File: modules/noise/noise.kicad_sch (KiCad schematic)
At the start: 25 parts, among them U1 ATtiny1616-M, U2 MCP6002-xSN, U3 MCP6002-xSN

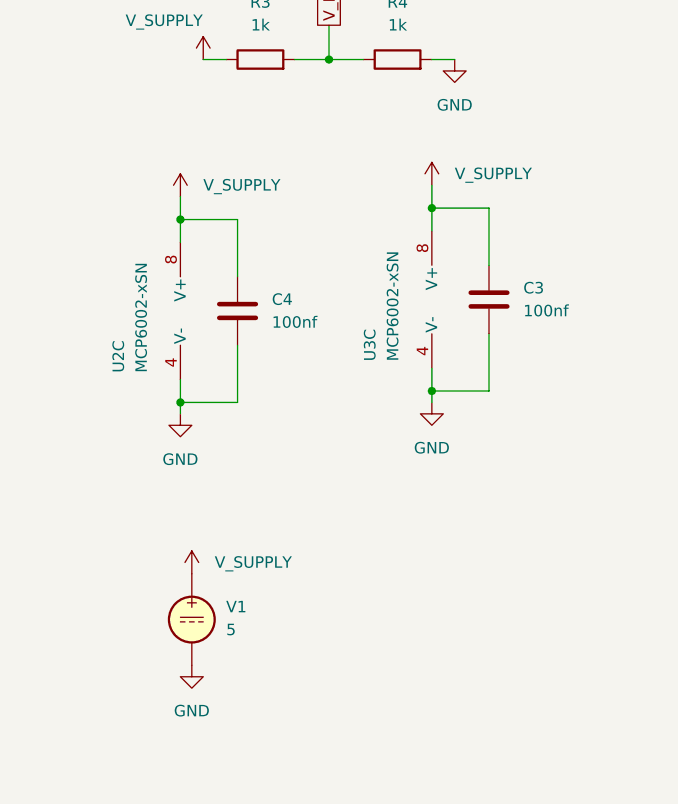
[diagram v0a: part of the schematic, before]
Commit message: Implement the PCB routing
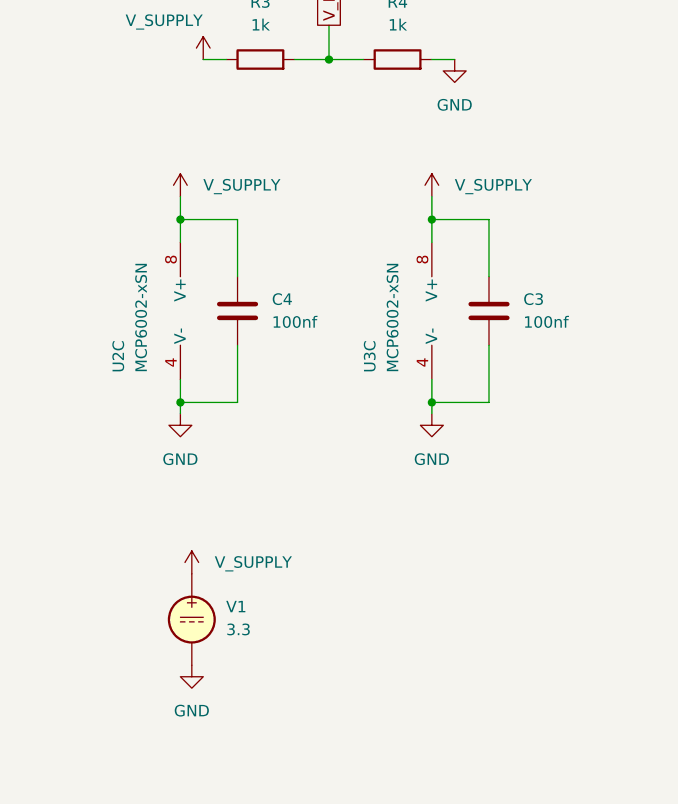
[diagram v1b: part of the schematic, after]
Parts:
- C1: footprint (none) -> Capacitor_SMD:C_1206_3216Metric
- C2, C3, C4, C5, C6: footprint (none) -> Capacitor_SMD:C_0402_1005Metric
- R1, R2, R3, R4, R5, R6, R7, R8: footprint (none) -> Resistor_SMD:R_0402_1005Metric
- RV1, RV2, RV3: footprint (none) -> BreadModular_Pots:Potentiometer_RV09
- U2, U3: footprint (none) -> Package_SO:SOIC-8-1EP_3.9x4.9mm_P1.27mm_EP2.29x3mm
- V1: value 5 -> 3.3
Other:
- moved on the sheet: C3, U3C
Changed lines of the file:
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@@
 	)
 	(junction
-		(at 260.35 123.19)
+		(at 260.35 124.46)
 		(diameter 0)
 		(color 0 0 0 0)
@@
 	)
 	(junction
-		(at 260.35 102.87)
+		(at 260.35 104.14)
 		(diameter 0)
 		(color 0 0 0 0)
@@
 	(wire
 		(pts
-			(xy 260.35 123.19) (xy 260.35 124.46)
+			(xy 260.35 124.46) (xy 260.35 125.73)
 		)
 		(stroke
@@
 	(wire
 		(pts
-			(xy 266.7 109.22) (xy 266.7 102.87)
+			(xy 266.7 110.49) (xy 266.7 104.14)
 		)
 		(stroke
@@
 	(wire
 		(pts
-			(xy 260.35 120.65) (xy 260.35 123.19)
+			(xy 260.35 121.92) (xy 260.35 124.46)
 		)
 		(stroke
@@
 	(wire
 		(pts
-			(xy 266.7 102.87) (xy 260.35 102.87)
+			(xy 266.7 104.14) (xy 260.35 104.14)
 		)
 		(stroke
@@
 	(wire
 		(pts
-			(xy 260.35 100.33) (xy 260.35 102.87)
+			(xy 260.35 101.6) (xy 260.35 104.14)
 		)
 		(stroke
@@
 	(wire
 		(pts
-			(xy 266.7 123.19) (xy 260.35 123.19)
+			(xy 266.7 124.46) (xy 260.35 124.46)
 		)
 		(stroke
@@
 	(wire
 		(pts
-			(xy 260.35 102.87) (xy 260.35 105.41)
+			(xy 260.35 104.14) (xy 260.35 106.68)
 		)
 		(stroke
@@
 	(wire
 		(pts
-			(xy 266.7 116.84) (xy 266.7 123.19)
+			(xy 266.7 118.11) (xy 266.7 124.46)
 		)
 		(stroke
@@
 			)
 		)
-		(property "Footprint" ""
+		(property "Footprint" "Resistor_SMD:R_0402_1005Metric"
 			(at 241.3 88.138 90)
 			(effects
@@
 			)
 		)
-		(property "Footprint" ""
+		(property "Footprint" "Resistor_SMD:R_0402_1005Metric"
 			(at 97.79 133.858 90)
 			(effects
@@
 			)
 		)
-		(property "Value" "5"
+		(property "Value" "3.3"
 			(at 237.49 149.7301 0)
 			(effects
@@
 			)
 		)
-		(property "Footprint" ""
+		(property "Footprint" "BreadModular_Pots:Potentiometer_RV09"
 			(at 88.9 125.73 0)
 			(effects
@@
 			)
 		)
-		(property "Footprint" ""
+		(property "Footprint" "Resistor_SMD:R_0402_1005Metric"
 			(at 83.82 48.768 90)
 			(effects
@@
 			)
 		)
-		(property "Footprint" ""
+		(property "Footprint" "Package_SO:SOIC-8-1EP_3.9x4.9mm_P1.27mm_EP2.29x3mm"
 			(at 124.46 110.49 0)
 			(effects
@@
 			)
 		)
-		(property "Footprint" ""
+		(property "Footprint" "Resistor_SMD:R_0402_1005Metric"
 			(at 148.59 163.068 90)
 			(effects
@@
 			)
 		)
-		(property "Footprint" ""
+		(property "Footprint" "Package_SO:SOIC-8-1EP_3.9x4.9mm_P1.27mm_EP2.29x3mm"
 			(at 53.34 107.95 0)
 			(effects
@@
 			)
 		)
-		(property "Footprint" ""
+		(property "Footprint" "Capacitor_SMD:C_0402_1005Metric"
 			(at 80.01 106.9848 0)
 			(effects
@@
 			)
 		)
-		(property "Footprint" ""
+		(property "Footprint" "Capacitor_SMD:C_0402_1005Metric"
 			(at 237.7948 110.49 0)
 			(effects
@@
 			)
 		)
-		(property "Footprint" ""
+		(property "Footprint" "Resistor_SMD:R_0402_1005Metric"
 			(at 83.82 29.718 90)
 			(effects
@@
 	(symbol
 		(lib_id "Amplifier_Operational:MCP6002-xSN")
-		(at 262.89 113.03 0)
+		(at 262.89 114.3 0)
 		(unit 3)
 		(exclude_from_sim no)
@@
 		(dnp no)
 		(property "Reference" "U3"
-			(at 253.492 119.888 90)
+			(at 253.492 121.158 90)
 			(effects
 				(font
@@
 		)
 		(property "Value" "MCP6002-xSN"
-			(at 256.032 119.888 90)
+			(at 256.032 121.158 90)
 			(effects
 				(font
@@
 			)
 		)
-		(property "Footprint" ""
-			(at 262.89 113.03 0)
+		(property "Footprint" "Package_SO:SOIC-8-1EP_3.9x4.9mm_P1.27mm_EP2.29x3mm"
+			(at 262.89 114.3 0)
 			(effects
 				(font
@@
 		)
 		(property "Datasheet" "http://ww1.microchip.com/downloads/en/DeviceDoc/21733j.pdf"
-			(at 262.89 113.03 0)
+			(at 262.89 114.3 0)
 			(effects
 				(font
@@
 		)
 		(property "Description" "1MHz, Low-Power Op Amp, SOIC-8"
-			(at 262.89 113.03 0)
+			(at 262.89 114.3 0)
 			(effects
 				(font
@@
 			)
 		)
-		(property "Footprint" ""
+		(property "Footprint" "BreadModular_Pots:Potentiometer_RV09"
 			(at 85.09 66.04 0)
 			(effects
@@
 	(symbol
 		(lib_id "power:GND")
-		(at 260.35 124.46 0)
+		(at 260.35 125.73 0)
 		(unit 1)
 		(exclude_from_sim no)
@@
 		(dnp no)
 		(property "Reference" "#PWR012"
-			(at 260.35 130.81 0)
+			(at 260.35 132.08 0)
 			(effects
 				(font
@@
 		)
 		(property "Value" "GND"
-			(at 260.35 129.54 0)
+			(at 260.35 130.81 0)
 			(effects
 				(font
@@
 		)
 		(property "Footprint" ""
-			(at 260.35 124.46 0)
+			(at 260.35 125.73 0)
 			(effects
 				(font
@@
 		)
 		(property "Datasheet" ""
-			(at 260.35 124.46 0)
+			(at 260.35 125.73 0)
 			(effects
 				(font
@@
 		)
 		(property "Description" "Power symbol creates a global label with name \"GND\" , ground"
-			(at 260.35 124.46 0)
+			(at 260.35 125.73 0)
 			(effects
 				(font
@@
 			)
 		)
-		(property "Footprint" ""
+		(property "Footprint" "Package_SO:SOIC-8-1EP_3.9x4.9mm_P1.27mm_EP2.29x3mm"
 			(at 129.54 161.29 0)
 			(effects
@@
 	(symbol
 		(lib_id "power:+5V")
-		(at 260.35 100.33 0)
+		(at 260.35 101.6 0)
 		(unit 1)
 		(exclude_from_sim no)
@@
 		(fields_autoplaced yes)
 		(property "Reference" "#PWR010"
-			(at 260.35 104.14 0)
+			(at 260.35 105.41 0)
 			(effects
 				(font
@@
 		)
 		(property "Value" "V_SUPPLY"
-			(at 262.89 99.0599 0)
+			(at 262.89 100.3299 0)
 			(effects
 				(font
@@
 		)
 		(property "Footprint" ""
-			(at 260.35 100.33 0)
+			(at 260.35 101.6 0)
 			(effects
 				(font
@@
 		)
 		(property "Datasheet" ""
-			(at 260.35 100.33 0)
+			(at 260.35 101.6 0)
 			(effects
 				(font
@@
 		)
 		(property "Description" "Power symbol creates a global label with name \"+5V\""
-			(at 260.35 100.33 0)
+			(at 260.35 101.6 0)
 			(effects
 				(font
@@
 			)
 		)
-		(property "Footprint" ""
+		(property "Footprint" "Package_SO:SOIC-8-1EP_3.9x4.9mm_P1.27mm_EP2.29x3mm"
 			(at 234.95 114.3 0)
 			(effects
@@
 			)
 		)
-		(property "Footprint" ""
+		(property "Footprint" "Capacitor_SMD:C_0402_1005Metric"
 			(at 93.0148 176.53 0)
 			(effects
@@
 			)
 		)
-		(property "Footprint" ""
+		(property "Footprint" "Resistor_SMD:R_0402_1005Metric"
 			(at 143.51 112.268 90)
 			(effects
@@
 			)
 		)
-		(property "Footprint" ""
+		(property "Footprint" "Package_SO:SOIC-8-1EP_3.9x4.9mm_P1.27mm_EP2.29x3mm"
 			(at 52.07 161.29 0)
 			(effects
@@
 	(symbol
 		(lib_id "Device:C")
-		(at 266.7 113.03 180)
+		(at 266.7 114.3 180)
 		(unit 1)
 		(exclude_from_sim no)
@@
 		(fields_autoplaced yes)
 		(property "Reference" "C3"
-			(at 270.51 111.7599 0)
+			(at 270.51 113.0299 0)
 			(effects
 				(font
@@
 		)
 		(property "Value" "100nf"
-			(at 270.51 114.2999 0)
+			(at 270.51 115.5699 0)
 			(effects
 				(font
@@
 			)
 		)
-		(property "Footprint" ""
-			(at 265.7348 109.22 0)
+		(property "Footprint" "Capacitor_SMD:C_0402_1005Metric"
+			(at 265.7348 110.49 0)
 			(effects
 				(font
@@
 		)
 		(property "Datasheet" "~"
-			(at 266.7 113.03 0)
+			(at 266.7 114.3 0)
 			(effects
 				(font
@@
 		)
 		(property "Description" "Unpolarized capacitor"
-			(at 266.7 113.03 0)
+			(at 266.7 114.3 0)
 			(effects
 				(font
@@
 			)
 		)
-		(property "Footprint" ""
+		(property "Footprint" "BreadModular_Pots:Potentiometer_RV09"
 			(at 74.93 161.29 0)
 			(effects
@@
 			)
 		)
-		(property "Footprint" ""
+		(property "Footprint" "Resistor_SMD:R_0402_1005Metric"
 			(at 256.54 88.138 90)
 			(effects
@@
 			)
 		)
-		(property "Footprint" ""
+		(property "Footprint" "Capacitor_SMD:C_1206_3216Metric"
 			(at 45.72 26.9748 0)
 			(effects
@@
 			)
 		)
-		(property "Footprint" ""
+		(property "Footprint" "Resistor_SMD:R_0402_1005Metric"
 			(at 85.09 169.418 90)
 			(effects
@@
 			)
 		)
-		(property "Footprint" ""
+		(property "Footprint" "Capacitor_SMD:C_0402_1005Metric"
 			(at 93.0148 168.91 0)
 			(effects
